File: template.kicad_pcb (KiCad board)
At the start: 2 copper layers, 40 x 22.5 mm, 2 parts, among them J1 Screw Terminal Block 5.00 mm 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

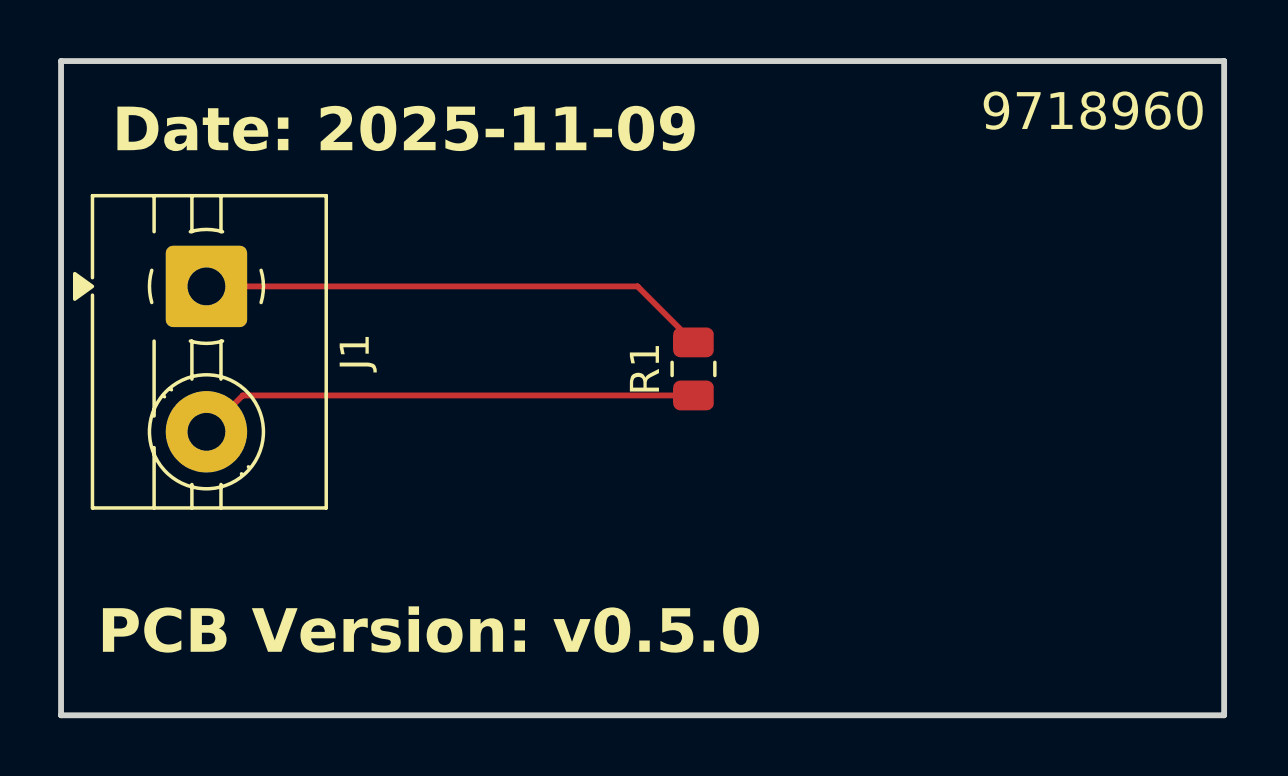
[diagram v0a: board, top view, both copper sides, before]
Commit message: feat: add OpenPnP position file export with top/bottom split
Add KiBot position output for pick and place machines (OpenPnP),
generating separate CSV files for top and bottom SMD populated
components. Also add connector_board test design and update template
schematic/PCB with bottom-side components for testing.

Co-Authored-By: Claude Opus 4.6 <noreply@anthropic.com>
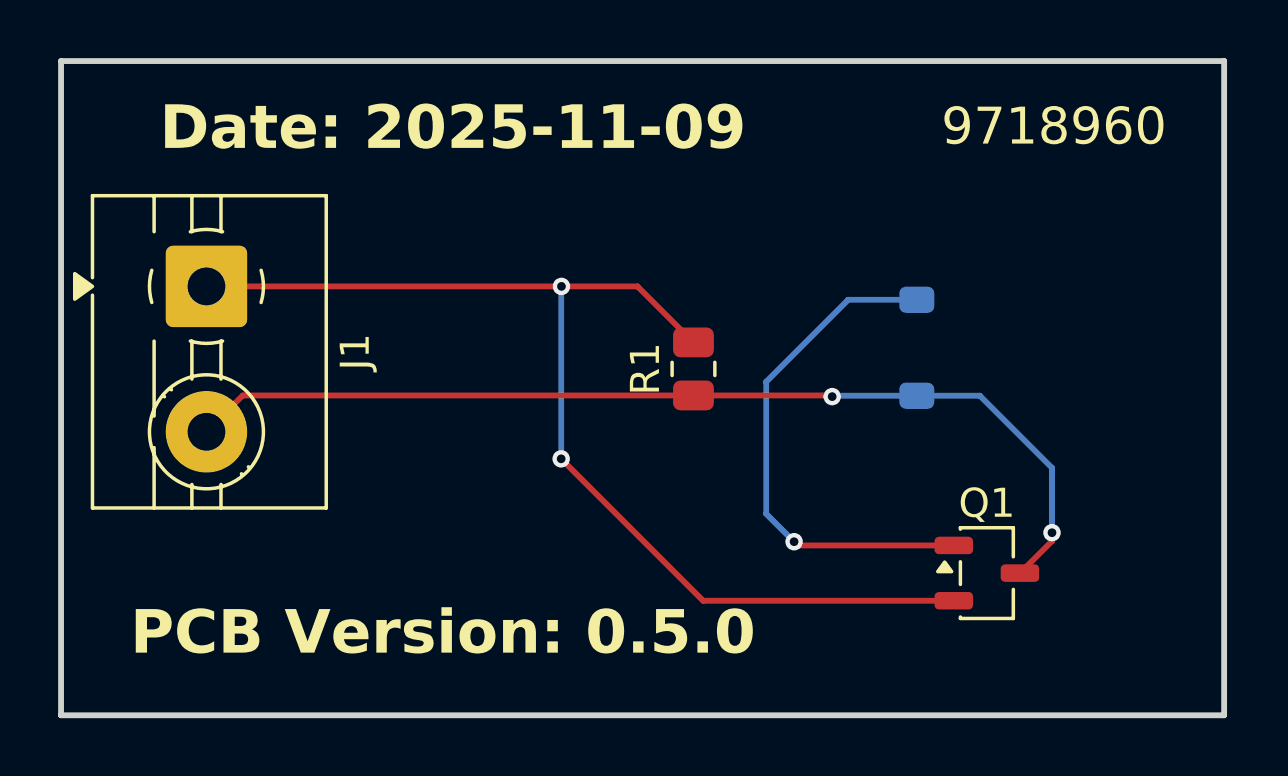
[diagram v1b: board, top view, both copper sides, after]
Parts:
- added D1: MBR0530, Diode_SMD:D_SOD-123, B.Cu at (168.7, 61.4)
- added Q1: BSS138, Package_TO_SOT_SMD:SOT-23-3, F.Cu at (171.1, 69.1)
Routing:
- net GND: track 17.5 -> 39.0 mm, vias 0 -> 2
- net Net-(D1-K): track 0.00 -> 17.8 mm, vias 0 -> 1
- net Net-(D1-A): track 17.3 -> 34.7 mm, vias 0 -> 2
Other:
- board text added: "PCB Version: ${REVISION}"
- board text removed: "PCB Version: v${REVISION}"
